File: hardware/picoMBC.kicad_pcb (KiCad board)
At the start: 2 copper layers, 100 x 145 mm, 40 parts, among them J1 MicroSD, J2 Conn_02x25_Odd_Even, U1 Pico 2, U2 74LS125

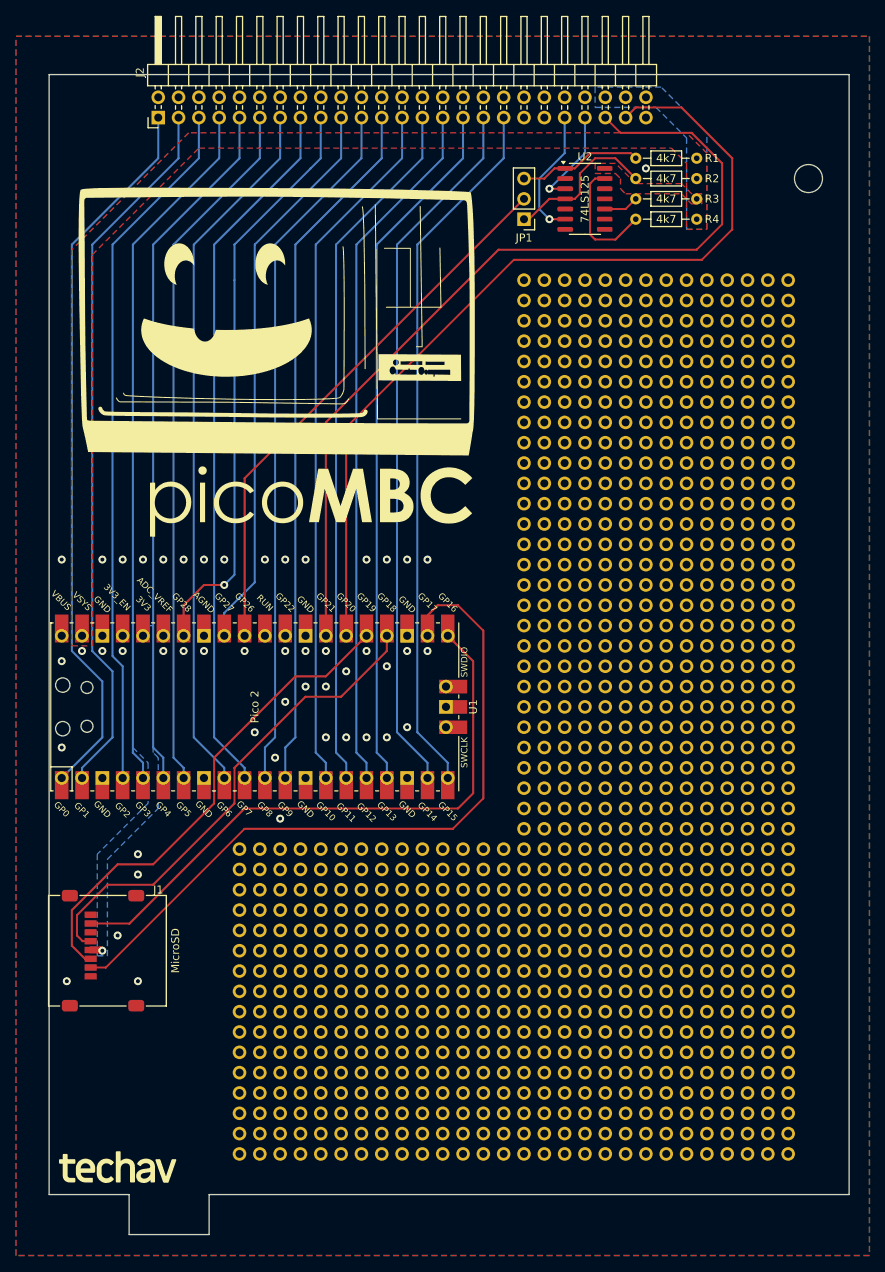
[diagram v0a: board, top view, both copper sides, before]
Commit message: Multiplex pico bus
- add buffers to multiplex Pico bus to free up some I/O for future use
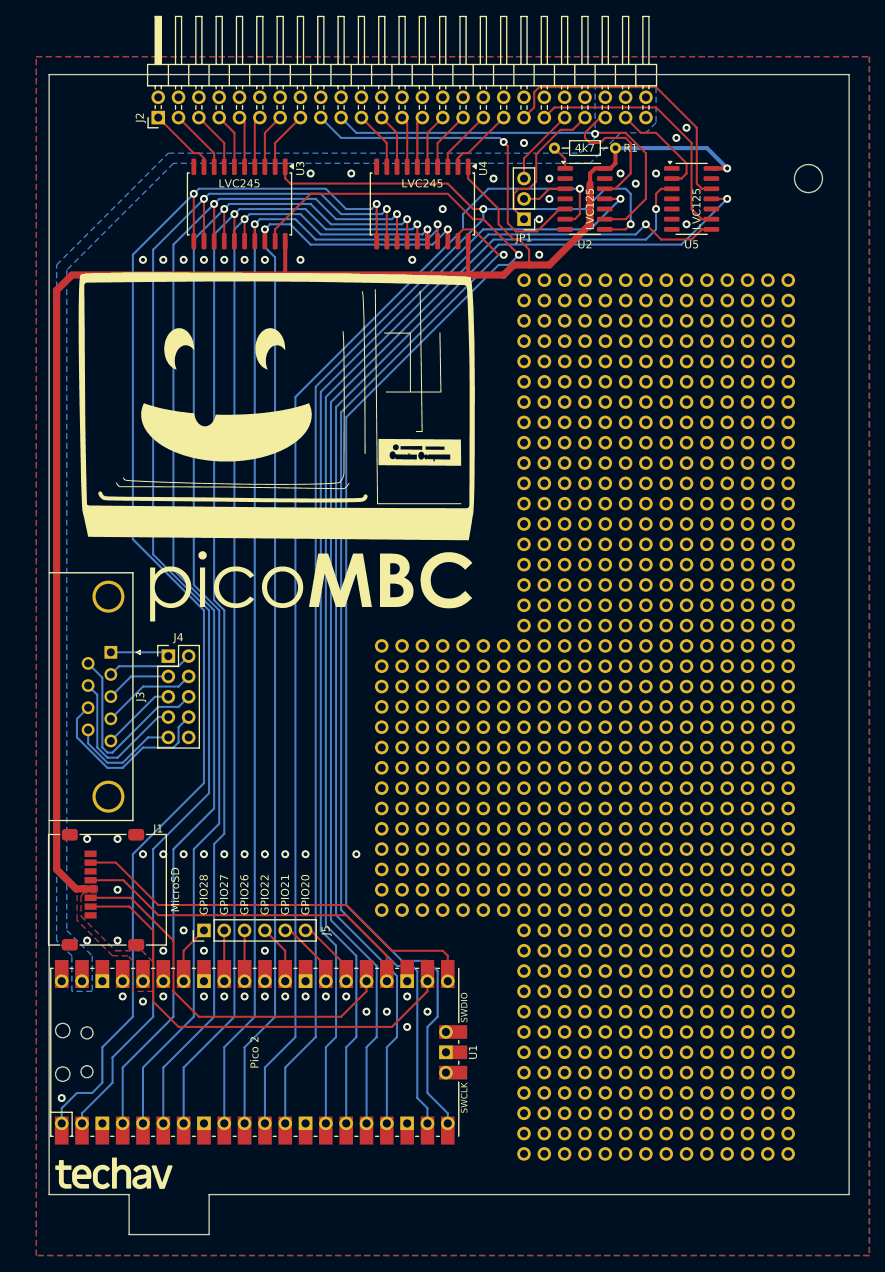
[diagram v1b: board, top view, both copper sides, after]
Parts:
- removed R2, R3, R4: 4k7, Resistor_THT:R_Axial_DIN0204_L3.6mm_D1.6mm_P7.62mm_Horizontal
- removed the REF** at (111.8, 66.0)
- removed the REF** at (111.8, 71.1)
- removed the REF** at (76.2, 147.3)
- removed the REF** at (76.2, 162.6)
- removed the REF** at (76.2, 172.7)
- removed the REF** at (76.2, 137.2)
- removed the REF** at (76.2, 167.6)
- removed the REF** at (76.2, 152.4)
- removed the REF** at (111.8, 76.2)
- removed the REF** at (76.2, 157.5)
- removed the REF** at (76.2, 142.2)
- added J3: DE9_Plug_MountingHoles, Connector_Dsub:DSUB-9_Male_Horizontal_P2.77x2.84mm_EdgePinOffset4.94mm_Housed_MountingHolesOffset7.48mm, F.Cu at (60.1, 110.0)
- added J4: Conn_02x05_Odd_Even, Connector_PinHeader_2.54mm:PinHeader_2x05_P2.54mm_Vertical, F.Cu at (67.3, 110.5)
- added J5: Conn_01x06, Connector_PinHeader_2.54mm:PinHeader_1x06_P2.54mm_Vertical, F.Cu at (71.8, 144.8)
- added REF**: PinHeader_2x07_P2.54mm_Vertical, Connector_PinHeader_2.54mm:PinHeader_2x07_P2.54mm_Vertical, F.Cu at (94.0, 137.2)
- added REF**: PinHeader_2x07_P2.54mm_Vertical, Connector_PinHeader_2.54mm:PinHeader_2x07_P2.54mm_Vertical, F.Cu at (94.0, 111.8)
- added REF**: PinHeader_2x14_P2.54mm_Vertical, Connector_PinHeader_2.54mm:PinHeader_2x14_P2.54mm_Vertical, F.Cu at (111.8, 71.1)
- added REF**: PinHeader_2x07_P2.54mm_Vertical, Connector_PinHeader_2.54mm:PinHeader_2x07_P2.54mm_Vertical, F.Cu at (94.0, 142.2)
- added REF**: PinHeader_2x07_P2.54mm_Vertical, Connector_PinHeader_2.54mm:PinHeader_2x07_P2.54mm_Vertical, F.Cu at (94.0, 116.8)
- added REF**: PinHeader_2x14_P2.54mm_Vertical, Connector_PinHeader_2.54mm:PinHeader_2x14_P2.54mm_Vertical, F.Cu at (111.8, 66.0)
- added REF**: PinHeader_2x14_P2.54mm_Vertical, Connector_PinHeader_2.54mm:PinHeader_2x14_P2.54mm_Vertical, F.Cu at (111.8, 76.2)
- added REF**: PinHeader_2x07_P2.54mm_Vertical, Connector_PinHeader_2.54mm:PinHeader_2x07_P2.54mm_Vertical, F.Cu at (94.0, 127.0)
- added REF**: PinHeader_2x07_P2.54mm_Vertical, Connector_PinHeader_2.54mm:PinHeader_2x07_P2.54mm_Vertical, F.Cu at (94.0, 121.9)
- added REF**: PinHeader_2x07_P2.54mm_Vertical, Connector_PinHeader_2.54mm:PinHeader_2x07_P2.54mm_Vertical, F.Cu at (94.0, 132.1)
- added U3: 74LVC245AD,118, Package_SO:SOIC-20W_7.5x12.8mm_P1.27mm, F.Cu at (76.2, 54.0)
- added U4: 74LVC245AD,118, Package_SO:SOIC-20W_7.5x12.8mm_P1.27mm, F.Cu at (99.1, 54.0)
- added U5: 74LVC125AD,118, Package_SO:SOIC-14_3.9x8.7mm_P1.27mm, F.Cu at (132.7, 53.3)
- U2: value 74LS125 -> 74LVC125AD,118
- moved U1 43.2 mm to (78.1, 160.0)
- moved R1 10.2 mm to (123.2, 47.0)
- moved J1 7.62 mm to (59.7, 139.7)
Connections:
- JP1 pad 1: /~{PICO_INT} -> /~{BUS_NMI}
- JP1 pad 2: /~{PICO-IRQ} -> /~{BUS_IRQ}
- JP1 pad 3: /~{PICO_NMI} -> /~{BUS_INT}
- R1 pad 1: +5V -> +3.3V
- R1 pad 2: /~{PICO_NMI} -> /~{PICO-IRQ}
- U1 pad 1: /BUS_D0 -> /PICO_AD0
- U1 pad 10: /BUS_D7 -> /PICO_AD7
- U1 pad 11: /BUS_A0 -> /~{PICO_WR}
- U1 pad 12: /BUS_A1 -> /~{PICO_RD}
- U1 pad 14: /BUS_A2 -> /~{PICO_IORQ}
- U1 pad 15: /BUS_A3 -> /PICO_CLOCK
- U1 pad 16: /BUS_A4 -> /~{PICO_M1}
- U1 pad 17: /BUS_A5 -> /~{PICO_RESET}
- U1 pad 19: /BUS_A6 -> /~{AOE}
- U1 pad 2: /BUS_D1 -> /PICO_AD1
- U1 pad 20: /BUS_A7 -> /~{DOE}
- U1 pad 26: /~{BUS_M1} -> /GPIO20
- U1 pad 27: /~{BUS_IORQ} -> /GPIO21
- U1 pad 29: unconnected-(U1-GPIO22-Pad29) -> /GPIO22
- U1 pad 31: /~{PICO-IRQ} -> /GPIO26
- U1 pad 32: /~{BUS_RD} -> /GPIO27
- U1 pad 34: /~{BUS_WR} -> /GPIO28
- U1 pad 4: /BUS_D2 -> /PICO_AD2
- U1 pad 5: /BUS_D3 -> /PICO_AD3
- U1 pad 6: /BUS_D4 -> /PICO_AD4
- U1 pad 7: /BUS_D5 -> /PICO_AD5
- U1 pad 9: /BUS_D6 -> /PICO_AD6
- U2 pad 1: /~{PICO_NMI} -> /~{PICO-IRQ}
- U2 pad 10: Net-(R3-Pad2) -> GND
- U2 pad 11: unconnected-(U2-Pad11) -> /~{PICO_IORQ}
- U2 pad 12: unconnected-(U2-Pad12) -> /~{BUS_IORQ}
- U2 pad 13: Net-(R4-Pad2) -> GND
- U2 pad 14: +5V -> +3.3V
- U2 pad 3: /~{BUS_NMI} -> /~{BUS_IRQ}
- U2 pad 4: /~{PICO_INT} -> GND
- U2 pad 5: GND -> /~{BUS_WR}
- U2 pad 6: /~{BUS_INT} -> /~{PICO_WR}
- U2 pad 8: unconnected-(U2-Pad8) -> /~{PICO_RD}
- U2 pad 9: unconnected-(U2-Pad9) -> /~{BUS_RD}
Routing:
- net +3.3V: track 1.50 -> 201.0 mm
- net /~{PICO_RD}: track 0.00 -> 179.4 mm, vias 0 -> 2
- net /PICO_AD0: track 0.00 -> 166.5 mm, vias 0 -> 2
- net /~{DOE}: track 0.00 -> 163.4 mm, vias 0 -> 1
- net /PICO_AD1: track 0.00 -> 161.4 mm, vias 0 -> 2
- net /PICO_AD2: track 0.00 -> 156.3 mm, vias 0 -> 2
- net /~{PICO_RESET}: track 0.00 -> 154.9 mm, vias 0 -> 1
- net /PICO_AD3: track 0.00 -> 152.3 mm, vias 0 -> 2
- net /PICO_CLOCK: track 0.00 -> 151.4 mm, vias 0 -> 1
- net /~{PICO_M1}: track 0.00 -> 149.3 mm, vias 0 -> 1
- net /PICO_AD4: track 0.00 -> 148.3 mm, vias 0 -> 2
- net /~{PICO_WR}: track 0.00 -> 145.1 mm, vias 0 -> 1
- net /PICO_AD5: track 0.00 -> 144.8 mm, vias 0 -> 2
- net /PICO_AD6: track 0.00 -> 143.5 mm, vias 0 -> 2
- net /~{PICO_IORQ}: track 0.00 -> 142.2 mm, vias 0 -> 1
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- added copper zone on F.Cu, net +3.3V
- removed copper zone on B.Cu, net +3.3V
- removed copper zone on F.Cu, net +5V
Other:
- board text added: "GPIO20"
- board text added: "GPIO21"
- board text added: "GPIO22"
- board text added: "GPIO26"
- board text added: "GPIO27"
- board text added: "GPIO28"
- board text added: "LVC125"
- board text added: "LVC245"

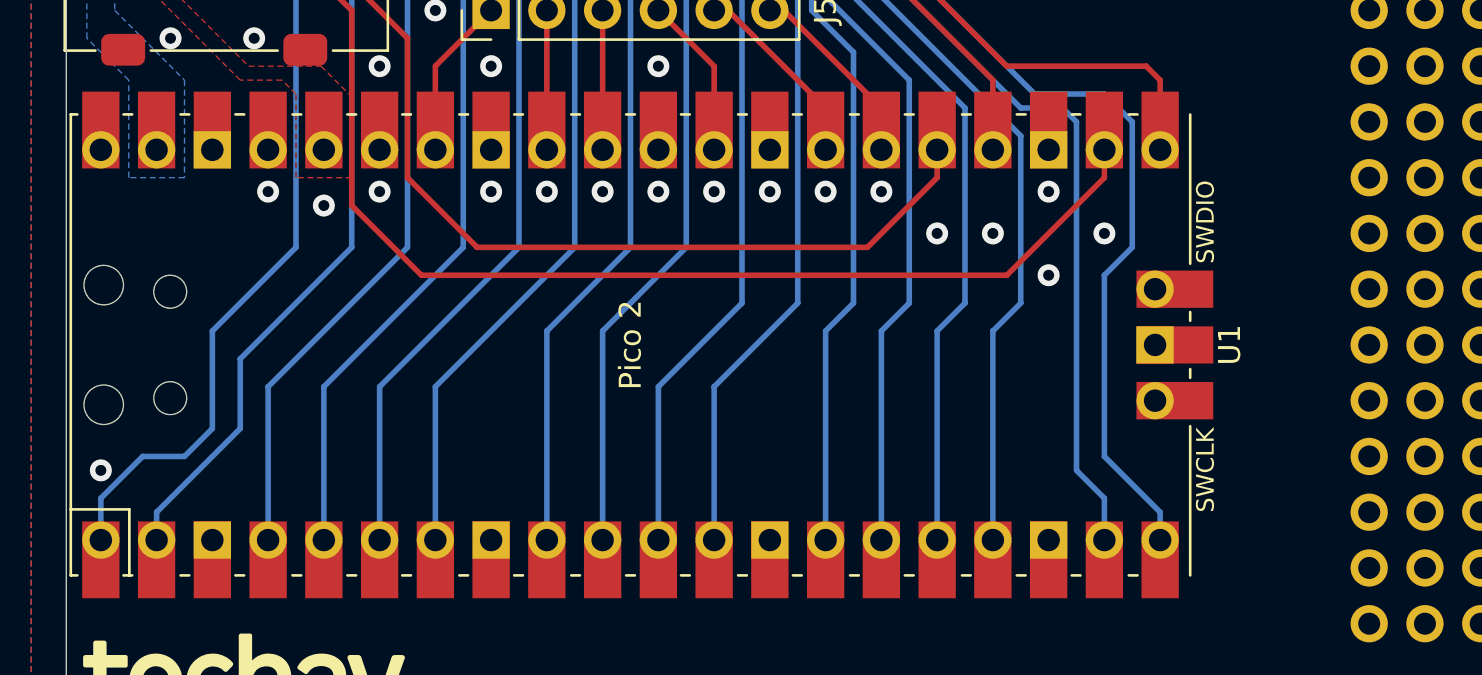
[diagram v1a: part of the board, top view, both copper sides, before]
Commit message: add power header & plot gerbers
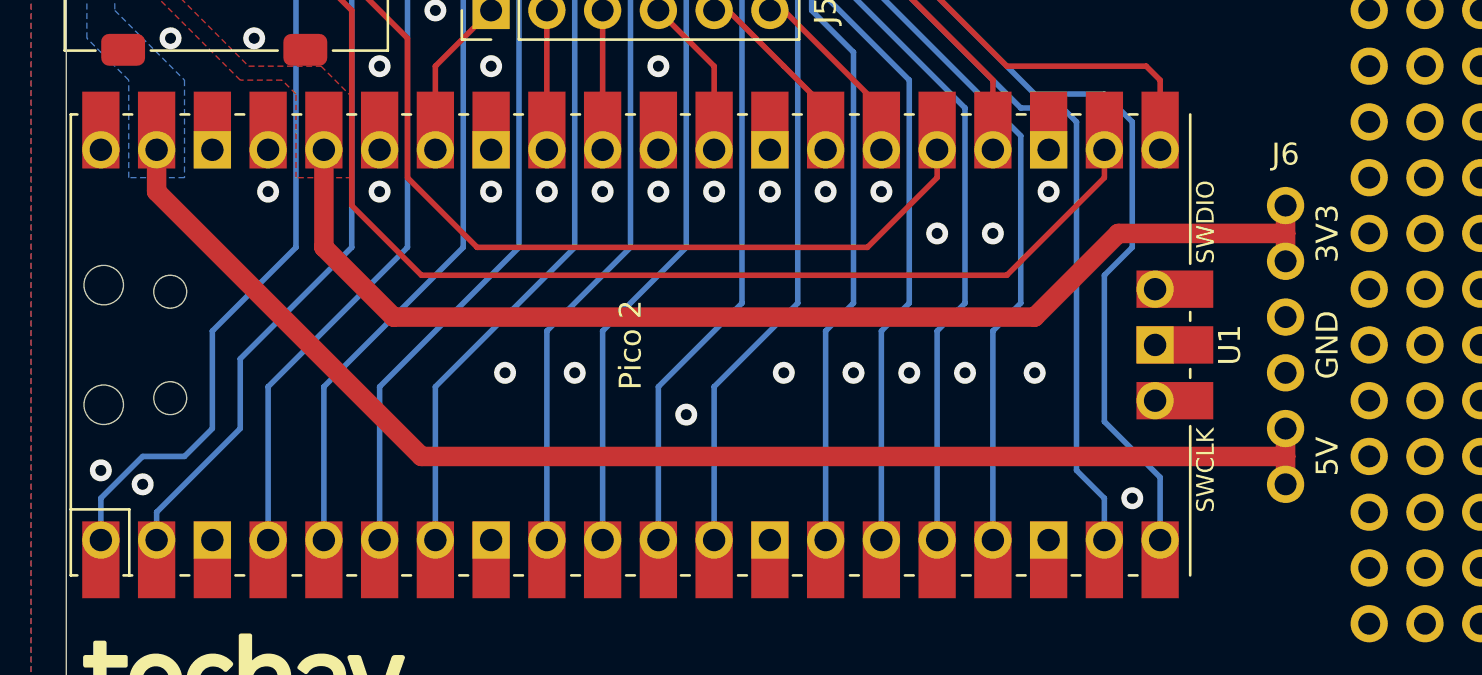
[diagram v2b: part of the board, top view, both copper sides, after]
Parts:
- added J6: Conn_01x06, Connector_PinHeader_2.54mm:PinHeader_1x06_P2.54mm_Vertical, F.Cu at (108.0, 153.7)
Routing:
- net +5V: track 0.00 -> 60.9 mm
- net +3.3V: track 201.0 -> 254.7 mm
- net GND: vias 60 -> 67
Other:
- board text added: "3V3"
- board text added: "5V"
- board text added: "GND"
